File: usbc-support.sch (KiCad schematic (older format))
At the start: 49 parts

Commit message: Started fixing DRC issues
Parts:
- C233, C234: renamed from C?; footprint (none) -> Capacitors_SMD:C_0603_HandSoldering
- R133, R134, R135, R136, R137, R138, R139, R140, R141, R142, R143, R144, R145, R146, R147, R148, R149, R150, R151: renamed from R?; footprint (none) -> Capacitors_SMD:C_0603_HandSoldering
- U11: renamed from U?; value LAN9514 -> LAN9514i; footprint (none) -> Housings_DFN_QFN:QFN-64-1EP_9x9mm_Pitch0.5mm
- gave numbers to parts that had none: 14
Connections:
- no-connect marks 42 -> 52

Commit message: Finished first pass on power distro, annotated USB C controllers
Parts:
- renumbered C233 to C?, C234 to C?, J33 to J?, J34 to J?, J1 to J?, R150 to R?, R151 to R?, R144 to R?, R145 to R?, R146 to R?, R147 to R?, R148 to R?, R149 to R?, R136 to R?, R137 to R?, R138 to R?, R139 to R?, R140 to R?, R141 to R?, R142 to R?, R143 to R?, R135 to R?, R133 to R?, R134 to R?, U14 to U0, U16 to U1, U18 to U2, U20 to U3, U22 to U4, U24 to U5, U26 to U6, U29 to U7, U12 to U?, U13 to U?, U11 to U?, U71 to U?

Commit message: Updated footprint assignments
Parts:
- C251, C252: renamed from C?; footprint Capacitors_SMD:C_0603_HandSoldering -> Capacitors_SMD:C_0603
- J33, J34: renamed from J?; footprint (none) -> Connect:USB_A
- R132, R133, R134, R135, R136, R137, R138, R139, R140, R141, R142, R143, R144, R145, R146, R147, R148, R149, R150: renamed from R?; footprint Capacitors_SMD:C_0603_HandSoldering -> Resistors_SMD:R_0603
- gave numbers to parts that had none: 5

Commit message: More work on pcb layout
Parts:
- R132, R133, R134, R135, R136, R137, R138, R139, R140, R141, R142, R143, R144, R145, R146, R147, R148, R149, R150: footprint Resistors_SMD:R_0603 -> Resistors_SMD:R_0402_NoSilk
- U0, U1, U2, U3, U4, U5, U6, U7: footprint SW-Texas:PBGA_96_ZQZ -> SW-Texas:TPS65982-ALT
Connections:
- net USB8_P: now reaches U12.21 (USB_UP_DP), U28.2 (USB2DP)
- net USB8_N: now reaches U12.22 (USB_UP_DN), U28.1 (USB2DN)
- net USB0_P: now reaches U0.L5 (USB_RP_P), U12.33 (USB_DN1_DP)
- net USB0_N: now reaches U0.K5 (USB_RP_N), U12.34 (USB_DN1_DN)
- net USB1_P: now reaches U1.L5 (USB_RP_P), U12.41 (USB_DN2_DP)
- net USB1_N: now reaches U1.K5 (USB_RP_N), U12.42 (USB_DN2_DN)
- net USB2_P: now reaches U12.49 (USB_DN3_DP), U2.L5 (USB_RP_P)
- net USB2_N: now reaches U12.50 (USB_DN3_DN), U2.K5 (USB_RP_N)
- net USB3_P: now reaches U12.56 (USB_DN4_DP), U3.L5 (USB_RP_P)
- net USB3_N: now reaches U12.57 (USB_DN4_DN), U3.K5 (USB_RP_N)
- net USB9_P: now reaches U24.21 (USB_UP_DP), U28.4 (USB3DP)
- net USB9_N: now reaches U24.22 (USB_UP_DN), U28.3 (USB3DN)
- net USB4_P: now reaches U24.33 (USB_DN1_DP), U4.L5 (USB_RP_P)
- net USB4_N: now reaches U24.34 (USB_DN1_DN), U4.K5 (USB_RP_N)
- net USB5_P: now reaches U24.41 (USB_DN2_DP), U5.L5 (USB_RP_P)
- net USB5_N: now reaches U24.42 (USB_DN2_DN), U5.K5 (USB_RP_N)
- net USB6_P: now reaches U24.49 (USB_DN3_DP), U6.L5 (USB_RP_P)
- net USB6_N: now reaches U24.50 (USB_DN3_DN), U6.K5 (USB_RP_N)
- net USB7_P: now reaches U24.56 (USB_DN4_DP), U7.L5 (USB_RP_P)
- net USB7_N: now reaches U24.57 (USB_DN4_DN), U7.K5 (USB_RP_N)
- net USB10_N: now reaches J33.2 (D-), U28.6 (USB4DN)
- net USB10_P: now reaches J33.3 (D+), U28.7 (USB4DP)
- net USB11_N: now reaches J34.2 (D-), U28.8 (USB5DN)
- net USB11_P: now reaches J34.3 (D+), U28.9 (USB5DP)
- net USBH_P: now reaches J1.165 (USB_DP), U28.59 (USB0DP)
- net USBH_N: now reaches J1.167 (USB_DN), U28.58 (USB0DN)
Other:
- moved on the sheet: U28A

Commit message: More work on pcb layout
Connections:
- net USBC-SCL: now reaches J1.30 (GPIO29), R149.1, U0.D2 (I2C_SCL1), U1.D2 (I2C_SCL1), U2.D2 (I2C_SCL1), U3.D2 (I2C_SCL1), U4.D2 (I2C_SCL1), U5.D2 (I2C_SCL1), U6.D2 (I2C_SCL1), U7.D2 (I2C_SCL1)
- net USBC-SDA: now reaches J1.28 (GPIO28), R150.1, U0.D1 (I2C_SDA1), U1.D1 (I2C_SDA1), U2.D1 (I2C_SDA1), U3.D1 (I2C_SDA1), U4.D1 (I2C_SDA1), U5.D1 (I2C_SDA1), U6.D1 (I2C_SDA1), U7.D1 (I2C_SDA1)
- net USBC-SDA2: now reaches R133.1, U0.A5 (I2C_SDA2), U1.A5 (I2C_SDA2), U2.A5 (I2C_SDA2), U3.A5 (I2C_SDA2), U4.A5 (I2C_SDA2), U5.A5 (I2C_SDA2), U6.A5 (I2C_SDA2), U7.A5 (I2C_SDA2)
- net USBC-SCL2: now reaches R132.1, U0.B5 (I2C_SCL2), U1.B5 (I2C_SCL2), U2.B5 (I2C_SCL2), U3.B5 (I2C_SCL2), U4.B5 (I2C_SCL2), U5.B5 (I2C_SCL2), U6.B5 (I2C_SCL2), U7.B5 (I2C_SCL2)
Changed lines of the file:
@@
 Text Label 11200 9000 0    60   ~ 0
 USBH_P
+Text Label 3050 3700 0    60   ~ 0
+USBC-SDA
+Text Label 3050 3600 0    60   ~ 0
+USBC-SCL
+Text Label 950  3600 1    60   ~ 0
+USBC-SCL2
+Text Label 1000 4250 1    60   ~ 0
+USBC-SDA2
 $EndSCHEMATC

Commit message: Even more pcb layout stuff. almost finished one usb c controller
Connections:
- net TX4-RX5: now reaches U4.E2 (UART_TX), U5.F2 (UART_RX)
- net TX3-RX4: now reaches U3.E2 (UART_TX), U4.F2 (UART_RX)
- net TX5-RX6: now reaches U5.E2 (UART_TX), U6.F2 (UART_RX)
- net TX6-RX7: now reaches U6.E2 (UART_TX), U7.F2 (UART_RX)
- net TX0-RX1: now reaches U0.E2 (UART_TX), U1.F2 (UART_RX)
- net RX0: now reaches R134.1, U0.F2 (UART_RX)
- net TX1-RX2: now reaches U1.E2 (UART_TX), U2.F2 (UART_RX)
- net TX2-RX3: now reaches U2.E2 (UART_TX), U3.F2 (UART_RX)
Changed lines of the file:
@@
 Text Label 1000 4250 1    60   ~ 0
 USBC-SDA2
+Text Label 1300 11950 1    60   ~ 0
+TX6-RX7
+Text Label 1300 10500 1    60   ~ 0
+TX5-RX6
+Text Label 1300 8950 1    60   ~ 0
+TX4-RX5
+Text Label 1300 7600 1    60   ~ 0
+TX3-RX4
+Text Label 1300 6100 1    60   ~ 0
+TX2-RX3
+Text Label 1300 4550 1    60   ~ 0
+TX1-RX2
+Text Label 1300 3000 1    60   ~ 0
+TX0-RX1
+Text Label 1300 1750 0    60   ~ 0
+RX0
 $EndSCHEMATC

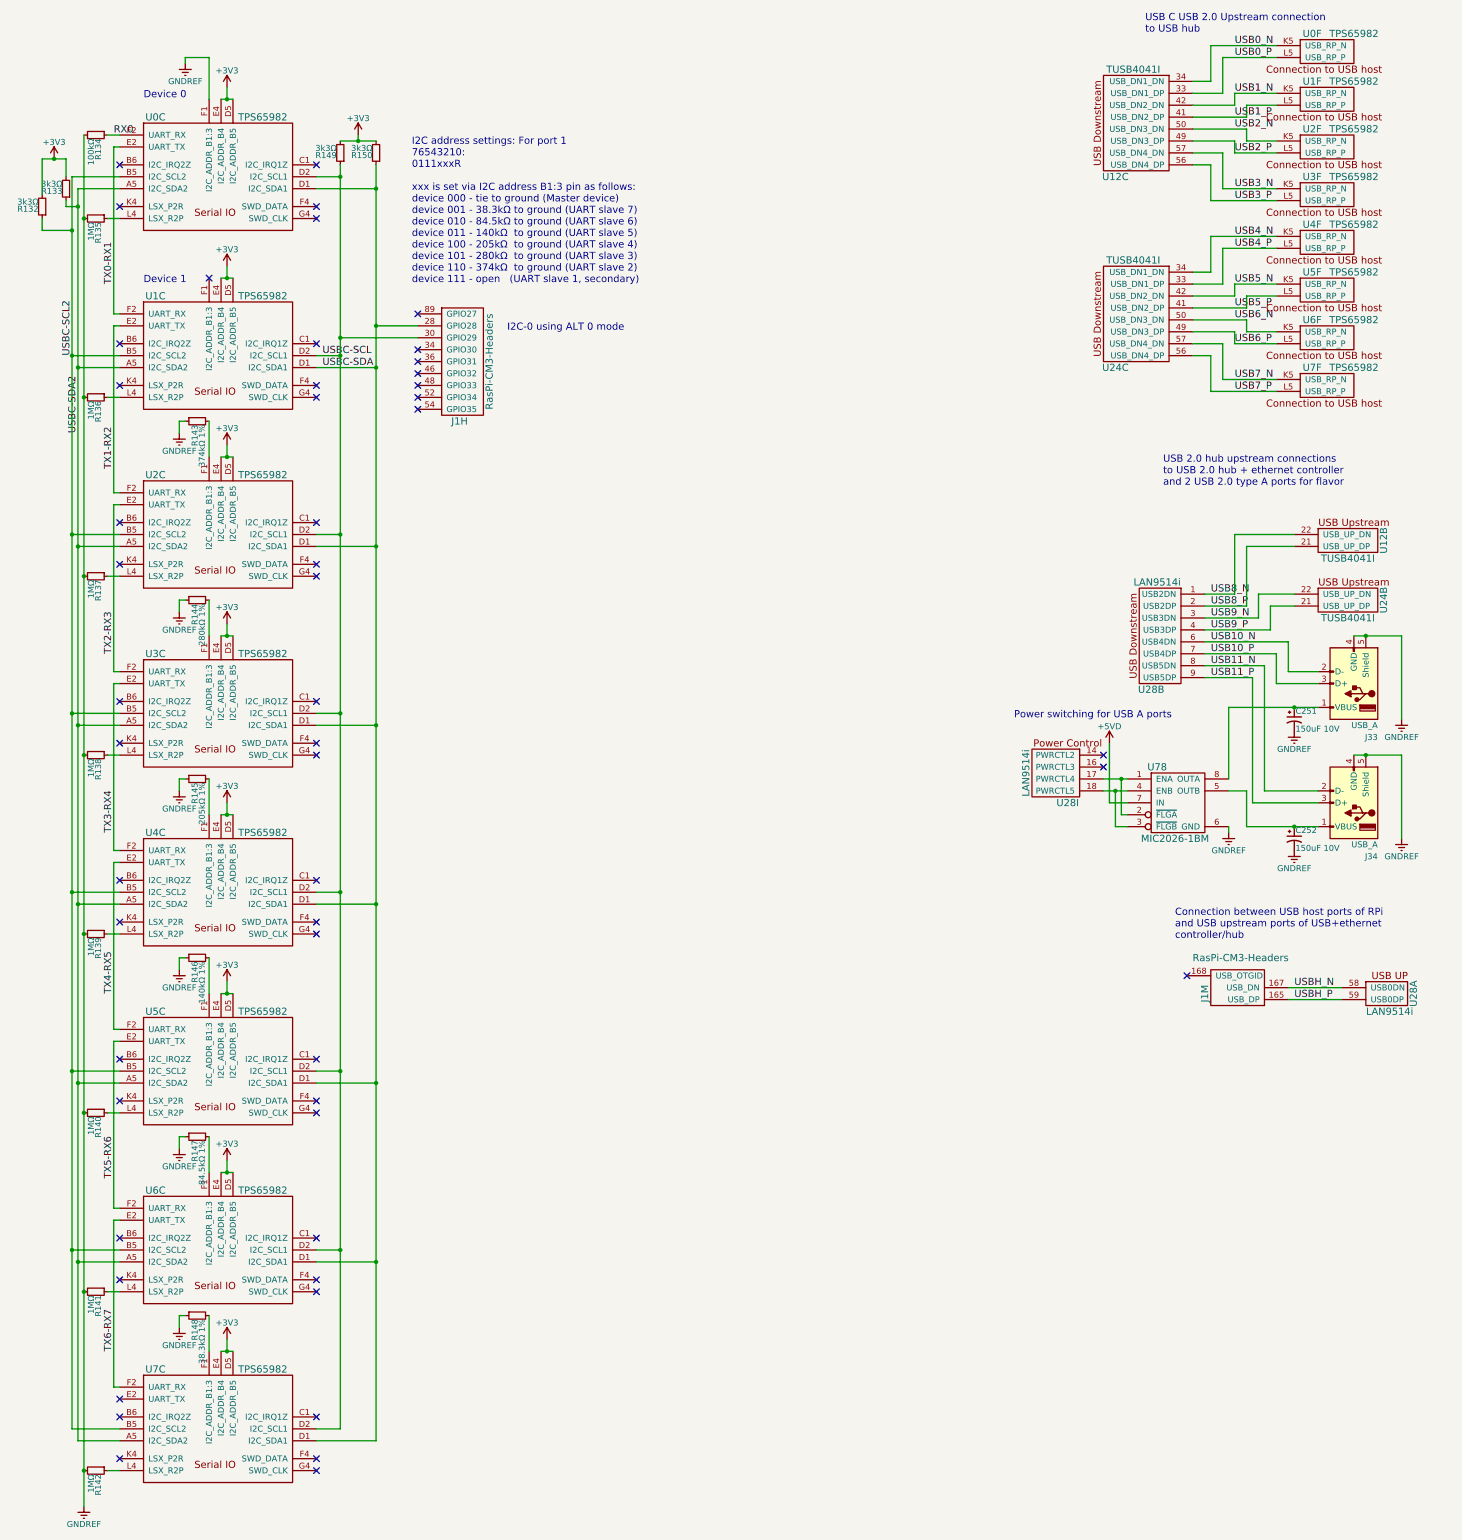
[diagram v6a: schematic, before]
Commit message: removed all traces of USB C trickery from this branch
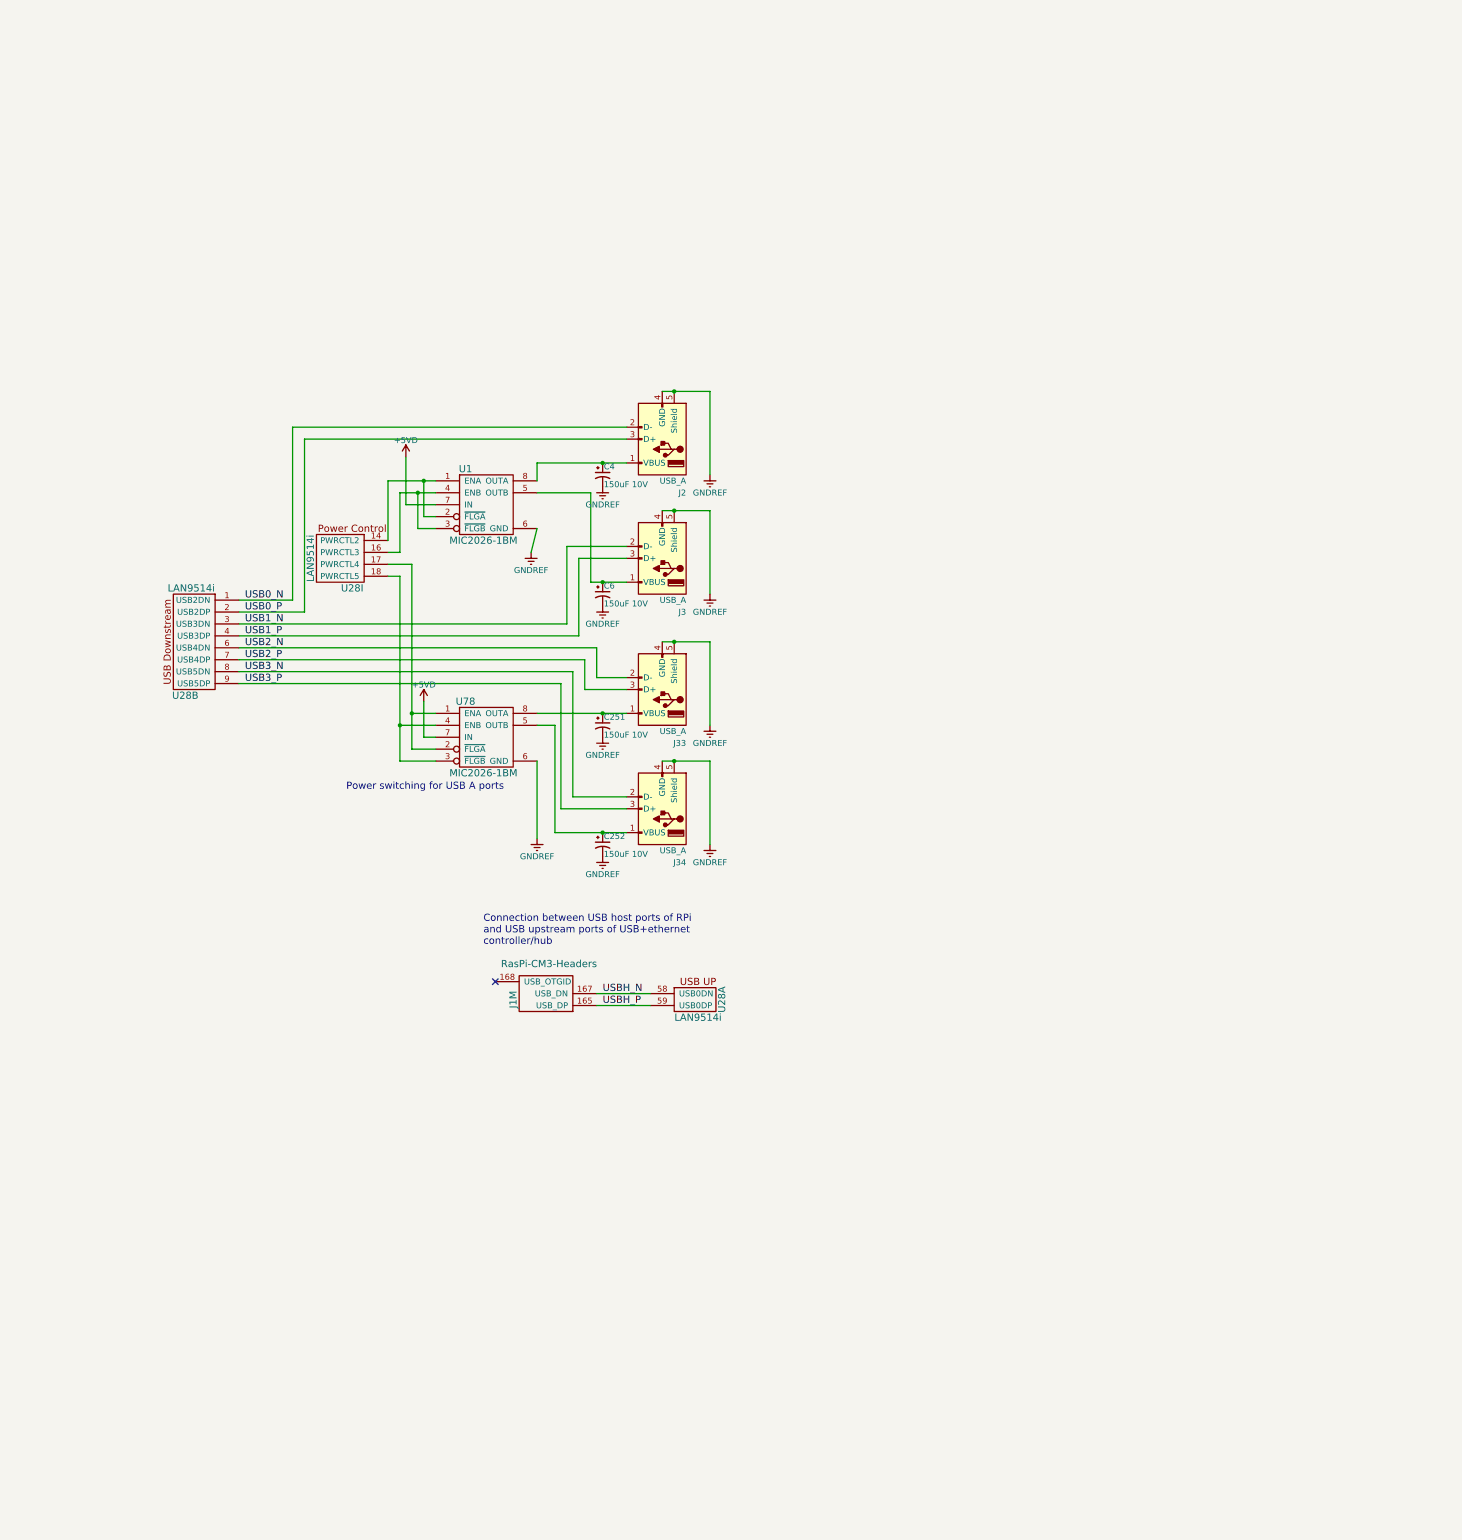
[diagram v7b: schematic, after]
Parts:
- removed unit 8 of J1
- removed R132, R133, R149, R150: 3k3Ω, Resistors_SMD:R_0402_NoSilk, symbol R_Small
- removed R134: 100kΩ, Resistors_SMD:R_0402_NoSilk, symbol R_Small
- removed R135, R136, R137, R138, R139, R140, R141, R142: 1MΩ, Resistors_SMD:R_0402_NoSilk, symbol R_Small
- removed R143: 374kΩ 1%, Resistors_SMD:R_0402_NoSilk, symbol R_Small
- removed R144: 280kΩ 1%, Resistors_SMD:R_0402_NoSilk, symbol R_Small
- removed R145: 205kΩ 1%, Resistors_SMD:R_0402_NoSilk, symbol R_Small
- removed R146: 140kΩ 1%, Resistors_SMD:R_0402_NoSilk, symbol R_Small
- removed R147: 84.5kΩ 1%, Resistors_SMD:R_0402_NoSilk, symbol R_Small
- removed R148: 38.3kΩ 1%, Resistors_SMD:R_0402_NoSilk, symbol R_Small
- removed U0, U1, U2, U3, U4, U5, U6, U7: TPS65982, SW-Texas:TPS65982-ALT, symbol TPS65982
- removed U12, U24: TUSB4041I, Housings_QFP:TQFP-64_1EP_10x10mm_Pitch0.5mm, symbol TUSB4041I
- added C4, C6: 150uF 10V, Capacitors_SMD:C_0603, symbol CP1_Small
- added J2, J3: USB_A, Connect:USB_A, symbol USB_A
- added U1: MIC2026-1BM, Housings_SOIC:SOIC-8_3.9x4.9mm_Pitch1.27mm, symbol MIC2026-1BM
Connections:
- net USB10_N is gone; now on net USB2_N: J33.2 (D-), U28.6 (USB4DN)
- net USB10_P is gone; now on net USB2_P: J33.3 (D+), U28.7 (USB4DP)
- net USB11_N is gone; now on net USB3_N: J34.2 (D-), U28.8 (USB5DN)
- net USB11_P is gone; now on net USB3_P: J34.3 (D+), U28.9 (USB5DP)
- net USB8_N is gone; now on net USB0_N: U28.1 (USB2DN)
- net USB8_P is gone; now on net USB0_P: U28.2 (USB2DP)
- net USB9_N is gone; now on net USB1_N: U28.3 (USB3DN)
- net USB9_P is gone; now on net USB1_P: U28.4 (USB3DP)
- net +5VD: now also U1.7 (IN)
- net GNDREF: now also C4.2, C6.2, J2.4 (GND), J2.5 (Shield), J3.4 (GND), J3.5 (Shield), U1.6 (GND)
- net USB0_N: now also J2.2 (D-)
- net USB0_P: now also J2.3 (D+)
- net USB1_N: now also J3.2 (D-)
- net USB1_P: now also J3.3 (D+)
- net at U28.14 (PWRCTL2): now also U1.1 (ENA), U1.2 (~FLGA)
- net at U28.16 (PWRCTL3): now also U1.3 (~FLGB), U1.4 (ENB)
- new net: C6.1, J3.1 (VBUS), U1.5 (OUTB)
- new net: C4.1, J2.1 (VBUS), U1.8 (OUTA)
- no-connect marks 52 -> 1
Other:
- note removed: "Device 0"
- note removed: "Device 1"
- note removed: "I2C address settings: For port 1\n76543210:\n0111xxxR\n\nxxx is set via I2C address B1:3 pin as follows:\ndevice 000 - tie to ground (Master device)\ndevice 001 - 38.3kΩ to ground (UART slave 7)\ndevice 010 - 84.5kΩ to ground (UART slave 6)\ndevice 011 - 140kΩ to ground (UART slave 5)\ndevice 100 - 205kΩ to ground (UART slave 4)\ndevice 101 - 280kΩ to ground (UART slave 3)\ndevice 110 - 374kΩ to 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"
- note removed: "I2C-0 using ALT 0 mode"
- note removed: "USB 2.0 hub upstream connections\nto USB 2.0 hub + ethernet controller\nand 2 USB 2.0 type A ports for flavor"
- note removed: "USB C USB 2.0 Upstream connection\nto USB hub"
- moved on the sheet: C251, C252, J1M, J33, J34, U28A, U28B, U28I, U78
